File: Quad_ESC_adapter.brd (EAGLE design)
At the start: 101.6 x 41.1 mm, 13 parts, among them J1 IBPD-SOCKET, J2 IBPD-SOCKET, J3 IBPD-SOCKET, J4 IBPD-SOCKET

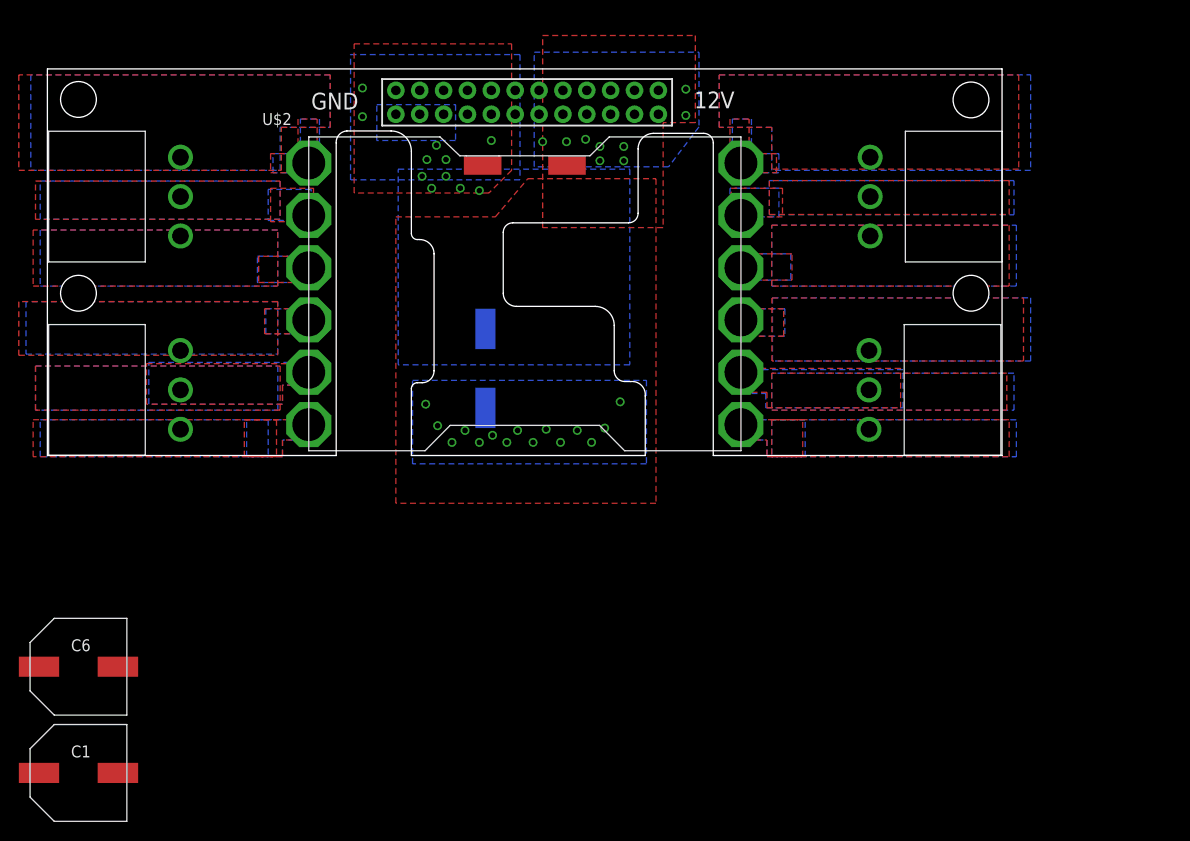
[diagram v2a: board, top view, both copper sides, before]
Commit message: added silkscreen, removed caps
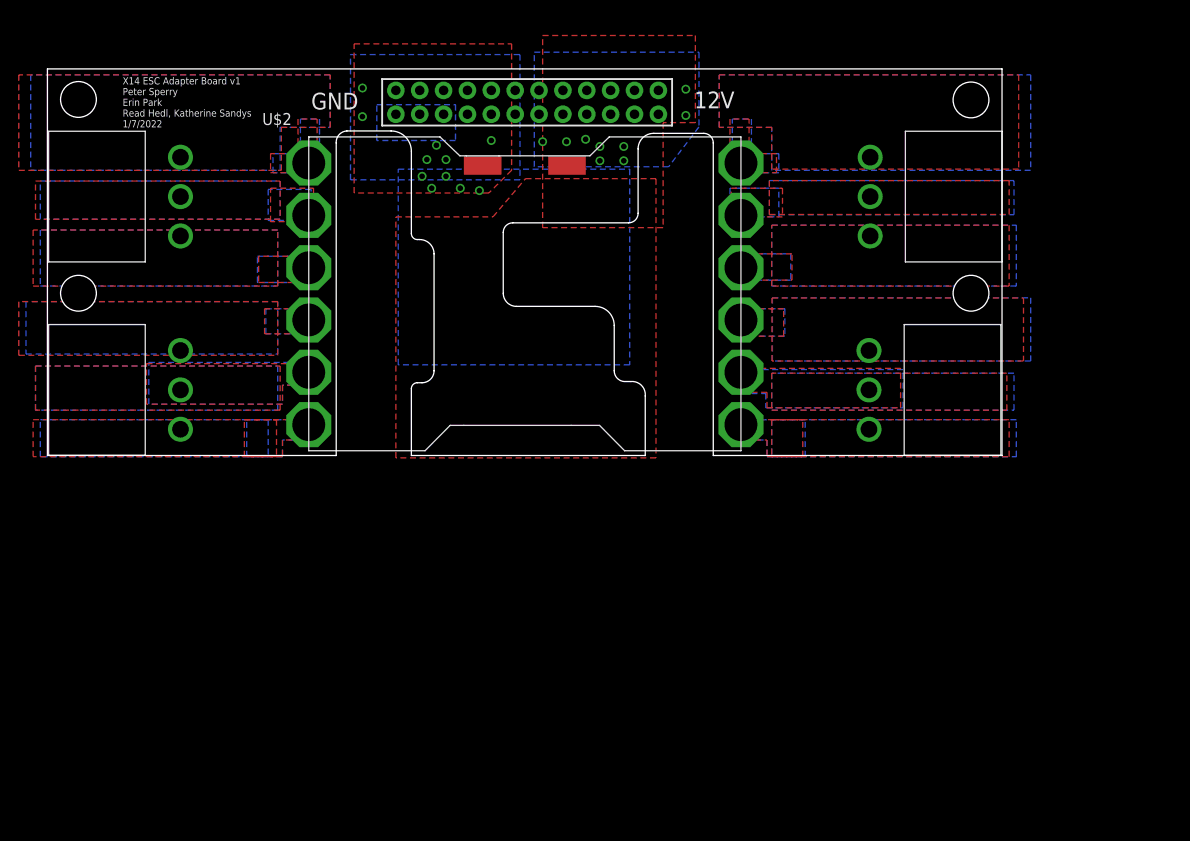
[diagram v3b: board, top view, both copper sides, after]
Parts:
- removed C1, C5, C6: 330uF, CAP, aluminin-capacitor-brick-UCM1H331MNL1GS:CAPAE1030X1050N
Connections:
- net 12V: no longer C1.+, C5.+, C6.+
- net GND: no longer C1.-, C5.-, C6.-
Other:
- board text added: "X14 ESC Adapter Board v1 Peter Sperry Erin Park Read Hedl, Katherine Sandys 1/7/2022"
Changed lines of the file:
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@@
 <?xml version="1.0" encoding="utf-8"?>
 <!DOCTYPE eagle SYSTEM "eagle.dtd">
-<eagle version="9.6.2">
+<eagle version="9.5.0">
 <drawing>
 <settings>
@@
 <text x="10.287" y="36.83" size="1.778" layer="25">GND</text>
 <text x="31.115" y="15.367" size="1.778" layer="26" rot="MR0">GND</text>
+<text x="-9.779" y="34.925" size="0.762" layer="25">X14 ESC Adapter Board v1
+Peter Sperry
+Erin Park
+Read Hedl, Katherine Sandys
+1/7/2022</text>
 </plain>
 <attributes>
@@
 <attribute name="NAME" x="5.08" y="35.179" size="1.27" layer="25"/>
 </element>
-<element name="C5" library="CAP, aluminin-capacitor-brick-UCM1H331MNL1GS" package="CAPAE1030X1050N" package3d_urn="urn:adsk.eagle:package:24202090/2" value="330uF" x="28.829" y="9.271" smashed="yes" rot="MR90">
-<attribute name="ARROW_PART_NUMBER" value="UCM1H331MNL1GS" x="28.829" y="9.271" size="1.778" layer="28" rot="MR90" display="off"/>
-<attribute name="ARROW_PRICE-STOCK" value="https://www.arrow.com/en/products/ucm1h331mnl1gs/nichicon" x="28.829" y="9.271" size="1.778" layer="28" rot="MR90" display="off"/>
-<attribute name="DESCRIPTION" value="Nichicon 330uF 50 V Aluminium Electrolytic Capacitor SMD, CM Series 2000h 10 (Dia.) x 10mm" x="28.829" y="9.271" size="1.778" layer="28" rot="MR90" display="off"/>
-<attribute name="HEIGHT" value="10.5mm" x="28.829" y="9.271" size="1.778" layer="28" rot="MR90" display="off"/>
-<attribute name="MANUFACTURER_NAME" value="Nichicon" x="28.829" y="9.271" size="1.778" layer="28" rot="MR90" display="off"/>
-<attribute name="MANUFACTURER_PART_NUMBER" value="UCM1H331MNL1GS" x="28.829" y="9.271" size="1.778" layer="28" rot="MR90" display="off"/>
-<attribute name="MOUSER_PART_NUMBER" value="647-UCM1H331MNL1GS" x="28.829" y="9.271" size="1.778" layer="28" rot="MR90" display="off"/>
-<attribute name="MOUSER_PRICE-STOCK" value="https://www.mouser.co.uk/ProductDetail/Nichicon/UCM1H331MNL1GS?qs=DSgADHjnLTkTovFLdbC%252BNg%3D%3D" x="28.829" y="9.271" size="1.778" layer="28" rot="MR90" display="off"/>
-<attribute name="NAME" x="31.115" y="9.525" size="1.27" layer="26" rot="MR90" align="center"/>
-<attribute name="VALUE" x="26.289" y="9.271" size="1.27" layer="28" rot="MR90" align="center"/>
-</element>
-<element name="C6" library="CAP, aluminin-capacitor-brick-UCM1H331MNL1GS" package="CAPAE1030X1050N" package3d_urn="urn:adsk.eagle:package:24202090/2" value="330uF" x="-14.478" y="-22.479" smashed="yes">
-<attribute name="ARROW_PART_NUMBER" value="UCM1H331MNL1GS" x="-14.478" y="-22.479" size="1.778" layer="27" display="off"/>
-<attribute name="ARROW_PRICE-STOCK" value="https://www.arrow.com/en/products/ucm1h331mnl1gs/nichicon" x="-14.478" y="-22.479" size="1.778" layer="27" display="off"/>
-<attribute name="DESCRIPTION" value="Nichicon 330uF 50 V Aluminium Electrolytic Capacitor SMD, CM Series 2000h 10 (Dia.) x 10mm" x="-14.478" y="-22.479" size="1.778" layer="27" display="off"/>
-<attribute name="HEIGHT" value="10.5mm" x="-14.478" y="-22.479" size="1.778" layer="27" display="off"/>
-<attribute name="MANUFACTURER_NAME" value="Nichicon" x="-14.478" y="-22.479" size="1.778" layer="27" display="off"/>
-<attribute name="MANUFACTURER_PART_NUMBER" value="UCM1H331MNL1GS" x="-14.478" y="-22.479" size="1.778" layer="27" display="off"/>
-<attribute name="MOUSER_PART_NUMBER" value="647-UCM1H331MNL1GS" x="-14.478" y="-22.479" size="1.778" layer="27" display="off"/>
-<attribute name="MOUSER_PRICE-STOCK" value="https://www.mouser.co.uk/ProductDetail/Nichicon/UCM1H331MNL1GS?qs=DSgADHjnLTkTovFLdbC%252BNg%3D%3D" x="-14.478" y="-22.479" size="1.778" layer="27" display="off"/>
-<attribute name="NAME" x="-14.224" y="-20.193" size="1.27" layer="25" align="center"/>
-<attribute name="VALUE" x="-14.478" y="-25.019" size="1.27" layer="27" align="center"/>
-</element>
-<element name="C1" library="CAP, aluminin-capacitor-brick-UCM1H331MNL1GS" package="CAPAE1030X1050N" package3d_urn="urn:adsk.eagle:package:24202090/2" value="330uF" x="-14.478" y="-33.782" smashed="yes">
-<attribute name="ARROW_PART_NUMBER" value="UCM1H331MNL1GS" x="-14.478" y="-33.782" size="1.778" layer="27" display="off"/>
-<attribute name="ARROW_PRICE-STOCK" value="https://www.arrow.com/en/products/ucm1h331mnl1gs/nichicon" x="-14.478" y="-33.782" size="1.778" layer="27" display="off"/>
-<attribute name="DESCRIPTION" value="Nichicon 330uF 50 V Aluminium Electrolytic Capacitor SMD, CM Series 2000h 10 (Dia.) x 10mm" x="-14.478" y="-33.782" size="1.778" layer="27" display="off"/>
-<attribute name="HEIGHT" value="10.5mm" x="-14.478" y="-33.782" size="1.778" layer="27" display="off"/>
-<attribute name="MANUFACTURER_NAME" value="Nichicon" x="-14.478" y="-33.782" size="1.778" layer="27" display="off"/>
-<attribute name="MANUFACTURER_PART_NUMBER" value="UCM1H331MNL1GS" x="-14.478" y="-33.782" size="1.778" layer="27" display="off"/>
-<attribute name="MOUSER_PART_NUMBER" value="647-UCM1H331MNL1GS" x="-14.478" y="-33.782" size="1.778" layer="27" display="off"/>
-<attribute name="MOUSER_PRICE-STOCK" value="https://www.mouser.co.uk/ProductDetail/Nichicon/UCM1H331MNL1GS?qs=DSgADHjnLTkTovFLdbC%252BNg%3D%3D" x="-14.478" y="-33.782" size="1.778" layer="27" display="off"/>
-<attribute name="NAME" x="-14.224" y="-31.496" size="1.27" layer="25" align="center"/>
-<attribute name="VALUE" x="-14.478" y="-36.322" size="1.27" layer="27" align="center"/>
-</element>
 </elements>
 <signals>
@@
 <vertex x="25.654" y="33.528"/>
 </polygon>
-<contactref element="C5" pad="-"/>
-<contactref element="C6" pad="-"/>
-<contactref element="C1" pad="-"/>
-<wire x1="-10.278" y1="-22.479" x2="-10.278" y2="-33.782" width="0" layer="19" extent="1-1"/>
-<wire x1="28.829" y1="13.471" x2="-10.278" y2="-22.479" width="0" layer="19" extent="1-16"/>
 </signal>
 <signal name="ESC4_B">
@@
 <vertex x="47.752" y="24.257"/>
 </polygon>
-<polygon width="0.508" layer="16" isolate="0.254">
-<vertex x="21.082" y="8.001"/>
-<vertex x="45.974" y="8.001"/>
-<vertex x="45.974" y="-0.889"/>
-<vertex x="21.082" y="-0.889"/>
-</polygon>
-<via x="23.749" y="3.175" extent="1-16" drill="0.6"/>
 <polygon width="0.6096" layer="16" isolate="0.254" thermals="no">
 <vertex x="34.036" y="42.926"/>
@@
 <vertex x="34.036" y="30.734"/>
 </polygon>
-<via x="22.479" y="5.461" extent="1-16" drill="0.6"/>
-<via x="25.273" y="1.397" extent="1-16" drill="0.6" alwaysstop="yes"/>
-<via x="26.67" y="2.667" extent="1-16" drill="0.6"/>
-<via x="28.194" y="1.397" extent="1-16" drill="0.6" alwaysstop="yes"/>
-<via x="29.591" y="2.159" extent="1-16" drill="0.6"/>
-<via x="31.115" y="1.397" extent="1-16" drill="0.6" alwaysstop="yes"/>
-<via x="32.258" y="2.667" extent="1-16" drill="0.6"/>
-<via x="33.909" y="1.397" extent="1-16" drill="0.6" alwaysstop="yes"/>
-<via x="35.306" y="2.794" extent="1-16" drill="0.6"/>
-<via x="36.83" y="1.397" extent="1-16" drill="0.6" alwaysstop="yes"/>
-<via x="38.608" y="2.667" extent="1-16" drill="0.6"/>
-<via x="40.132" y="1.397" extent="1-16" drill="0.6" alwaysstop="yes"/>
-<via x="41.529" y="2.921" extent="1-16" drill="0.6"/>
-<via x="43.18" y="5.715" extent="1-16" drill="0.6"/>
 <polygon width="0.508" layer="1" isolate="0.254">
 <vertex x="19.304" y="25.4"/>
-<vertex x="29.8958" y="25.4"/>
-<vertex x="33.3502" y="29.464"/>
+<vertex x="29.6418" y="25.4"/>
+<vertex x="33.0962" y="29.464"/>
 <vertex x="46.99" y="29.464"/>
-<vertex x="46.99" y="-5.08"/>
-<vertex x="19.304" y="-5.08"/>
+<vertex x="46.99" y="-0.254"/>
+<vertex x="19.304" y="-0.254"/>
 </polygon>
 <contactref element="U$2" pad="12V@4"/>
@@
 <via x="50.165" y="36.195" extent="1-16" drill="0.6" alwaysstop="yes"/>
 <via x="50.165" y="38.989" extent="1-16" drill="0.6" alwaysstop="yes"/>
-<contactref element="C5" pad="+"/>
-<contactref element="C6" pad="+"/>
-<contactref element="C1" pad="+"/>
-<wire x1="-18.678" y1="-22.479" x2="-18.678" y2="-33.782" width="0" layer="19" extent="1-1"/>
-<wire x1="23.749" y1="3.175" x2="-18.678" y2="-22.479" width="0" layer="19" extent="1-1"/>
 </signal>
 <signal name="ESC1_B">
@@
 </drawing>
 <compatibility>
+<note version="6.3" minversion="6.2.2" severity="warning">
+Since Version 6.2.2 text objects can contain more than one line,
+which will not be processed correctly with this version.
+</note>
 <note version="8.3" severity="warning">
 Since Version 8.3, EAGLE supports URNs for individual library
